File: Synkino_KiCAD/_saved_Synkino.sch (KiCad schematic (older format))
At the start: 155 parts, among them J1 Conn_01x02_Male, J10 EYE8_OUT, J11 EYE4_OUT, J12 2.5mm, J13 EYE5_OUT, J2 2.5mm, J3 3.5mm, J4 Micro_SD_Card_Det_Hirose_DM3AT, J5 EYE1_OUT, J6 EYE6_OUT, J7 EYE2_OUT, J8 EYE7_OUT, J9 EYE3_OUT, Q1 IRF7319, Q2 BC847, SW1 SW_Push, SW2 Rotary_Encoder_Switch, SW3 SW_Push, U1 MCP1702T-5002E/MB, U10 ATMEGA328P-AU, U11 QRE1113, U12 QRE1113, U13 QRE1113, U14 QRE1113, U15 QRE1113, U16 QRE1113, U18 QRE1113, U2 ATMEGA328P-AU, U3 74HC4050, U4 SPIOLED128x64, U5 AP7312-1833W6-7, U6 74HC14, U7 VS1053B, U8 MAX4741, U9 QRE1113, X1 FTDIconn, X2 ICSP, X3 FTDIconn, X4 ICSP, Y1 16Mhz, Y2 12.288MHz, Y3 16Mhz

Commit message: Everything connected
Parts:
- GND2: renamed from GND; footprint (none) -> Measurement_Points:Measurement_Point_Square-SMD-Pad_Small
- GNDA1: renamed from GNDA; footprint (none) -> Measurement_Points:Measurement_Point_Square-SMD-Pad_Small
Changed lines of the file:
@@
 	15200 4950 15300 4950
 $Comp
-L TEST GNDA
+L TEST GNDA1
 U 1 1 5AAC2C8C
 P 8250 4800
-F 0 "GNDA" H 8250 5100 50  0000 C BNN
+F 0 "GNDA1" H 8250 5100 50  0000 C BNN
 F 1 "GNDA" H 8250 5050 50  0000 C CNN
-F 2 "" H 8250 4800 50  0001 C CNN
+F 2 "Measurement_Points:Measurement_Point_Square-SMD-Pad_Small" H 8250 4800 50  0001 C CNN
 F 3 "" H 8250 4800 50  0001 C CNN
 	1    8250 4800
@@
 $EndComp
 $Comp
-L TEST GND
+L TEST GND2
 U 1 1 5AAC2E8C
 P 8050 4800
-F 0 "GND" H 8050 5100 50  0000 C BNN
+F 0 "GND2" H 8050 5100 50  0000 C BNN
 F 1 "GND" H 8050 5050 50  0000 C CNN
-F 2 "" H 8050 4800 50  0001 C CNN
+F 2 "Measurement_Points:Measurement_Point_Square-SMD-Pad_Small" H 8050 4800 50  0001 C CNN
 F 3 "" H 8050 4800 50  0001 C CNN
 	1    8050 4800

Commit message: Fixed the U1 footprint
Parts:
- U1: footprint TO_SOT_Packages_SMD:SOT-23 -> TO_SOT_Packages_SMD:SOT-89-3_Handsoldering
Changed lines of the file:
@@
 F 0 "U1" H 1400 1375 50  0000 C CNN
 F 1 "MCP1702T-5002E/MB" H 1550 1375 50  0000 L CNN
-F 2 "TO_SOT_Packages_SMD:SOT-23" H 1550 1450 50  0001 C CNN
+F 2 "TO_SOT_Packages_SMD:SOT-89-3_Handsoldering" H 1550 1450 50  0001 C CNN
 F 3 "" H 1550 1200 50  0001 C CNN
 	1    1550 1250

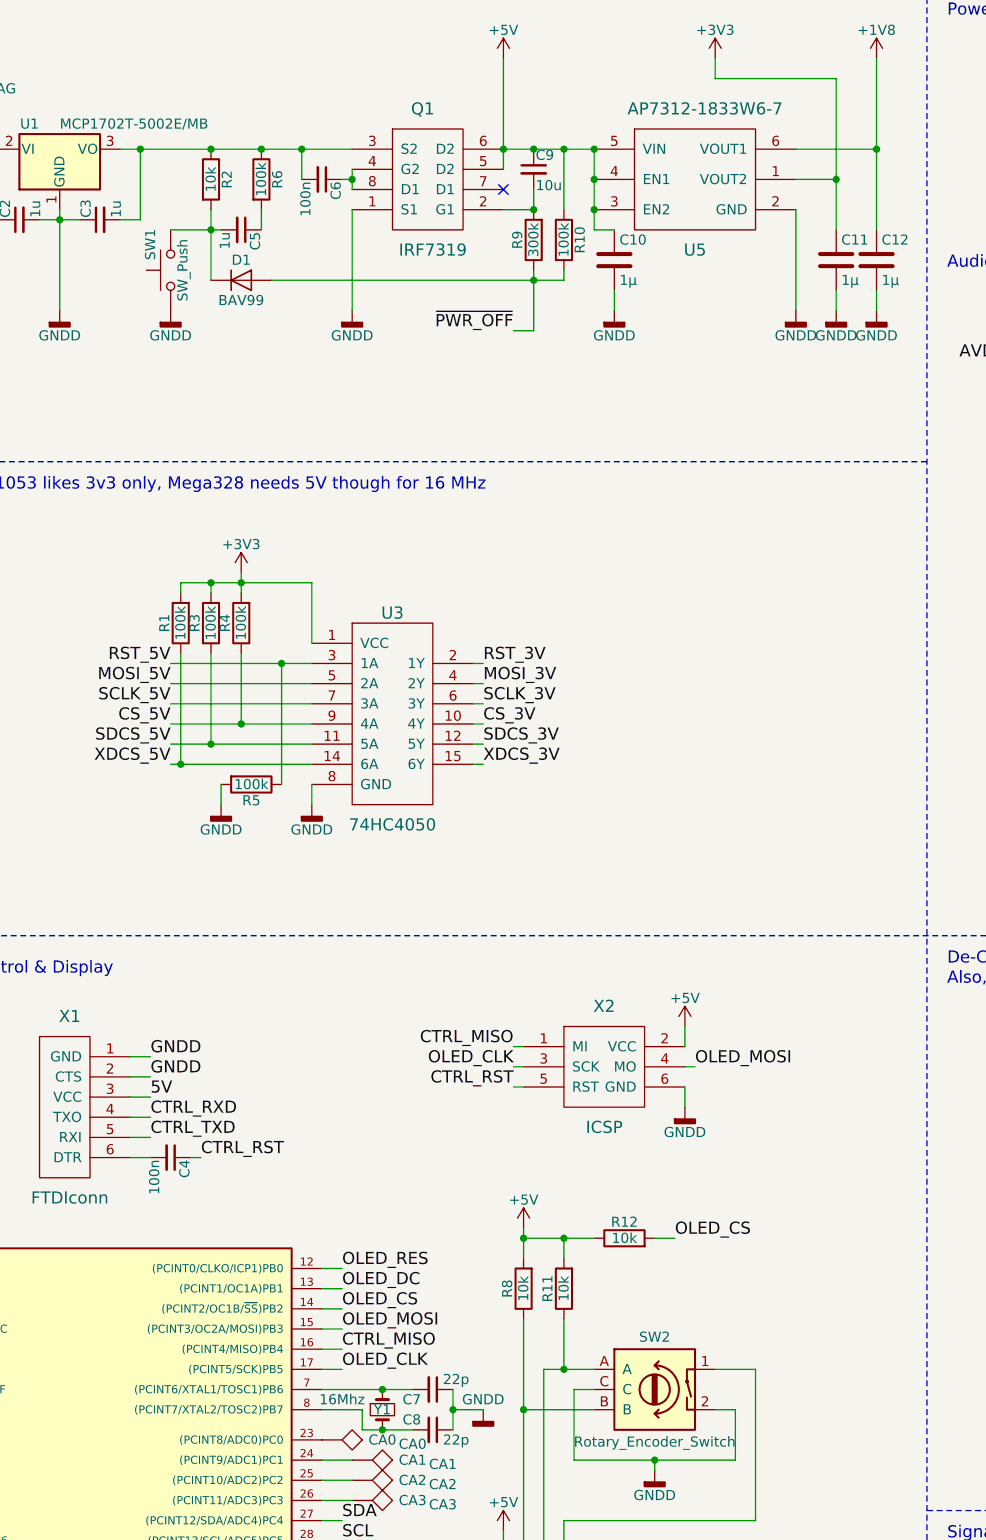
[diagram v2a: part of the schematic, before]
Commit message: More Ground Planes, Make Pwr Button optional
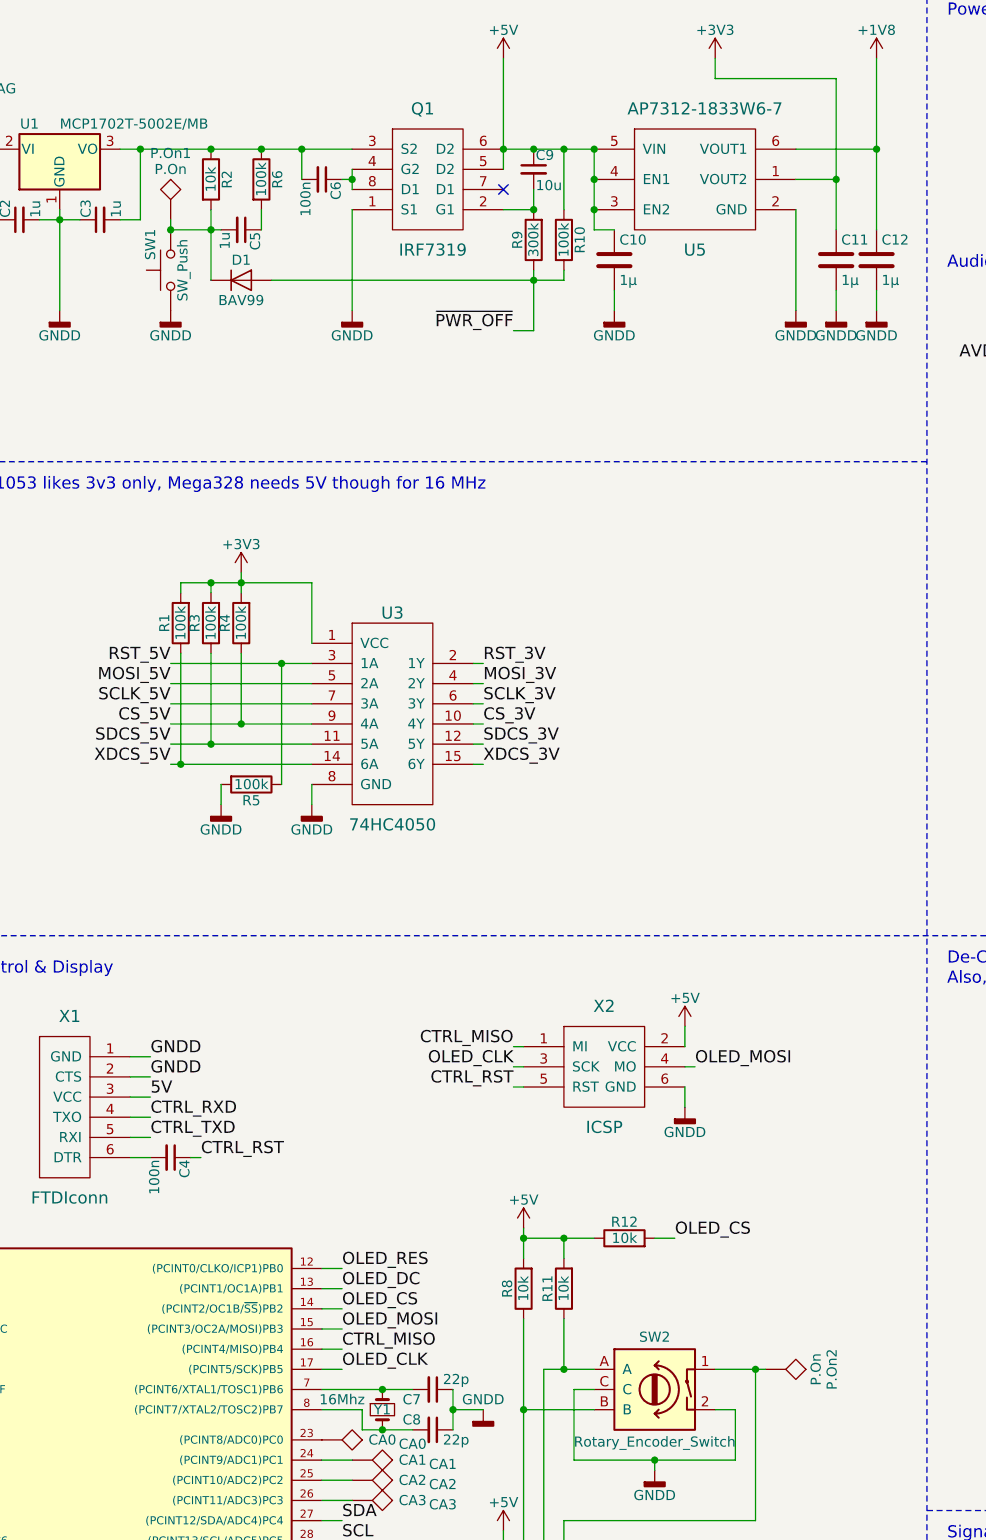
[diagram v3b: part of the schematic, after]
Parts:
- added P.On1, P.On2: P.On, Measurement_Points:Measurement_Point_Square-SMD-Pad_Small, symbol TEST
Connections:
- net at SW2.1, U2.2 ((PCINT20/XCK/T0)PD4): now also P.On2.1
- net at C5.2, D1.1 (K), R2.2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: now also P.On1.1
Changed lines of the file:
@@
 	4050 8050 5000 8050
 Wire Wire Line
-	5000 7300 4800 7300
+	4800 7300 5050 7300
 Wire Wire Line
 	2850 9000 2950 9000
@@
 Wire Wire Line
 	8250 4800 8250 4850
+$Comp
+L TEST P.On2
+U 1 1 5AAD7AE9
+P 5050 7300
+F 0 "P.On2" H 5050 7600 50  0000 C BNN
+F 1 "P.On" H 5050 7550 50  0000 C CNN
+F 2 "Measurement_Points:Measurement_Point_Square-SMD-Pad_Small" H 5050 7300 50  0001 C CNN
+F 3 "" H 5050 7300 50  0001 C CNN
+	1    5050 7300
+	0    1    1    0
+$EndComp
+$Comp
+L TEST P.On1
+U 1 1 5AAD7D0F
+P 2100 1600
+F 0 "P.On1" H 2100 1900 50  0000 C BNN
+F 1 "P.On" H 2100 1850 50  0000 C CNN
+F 2 "Measurement_Points:Measurement_Point_Square-SMD-Pad_Small" H 2100 1600 50  0001 C CNN
+F 3 "" H 2100 1600 50  0001 C CNN
+	1    2100 1600
+	1    0    0    -1
+$EndComp
+Connection ~ 5000 7300
+Wire Wire Line
+	2100 1600 2100 1650
+Connection ~ 2100 1650
 $EndSCHEMATC
